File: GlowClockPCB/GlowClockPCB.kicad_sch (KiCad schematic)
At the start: 52 parts, among them J1 LED_OUT_1, J2 LED_OUT_2, J3 LED_OUT_3, J4 LED_OUT_4, J5 POWER_IN, J6 Motor_1_Out, J7 Motor_2_Out, J8 I2C_LCD, J9 ADC_OUT, SW1 BTN_UP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

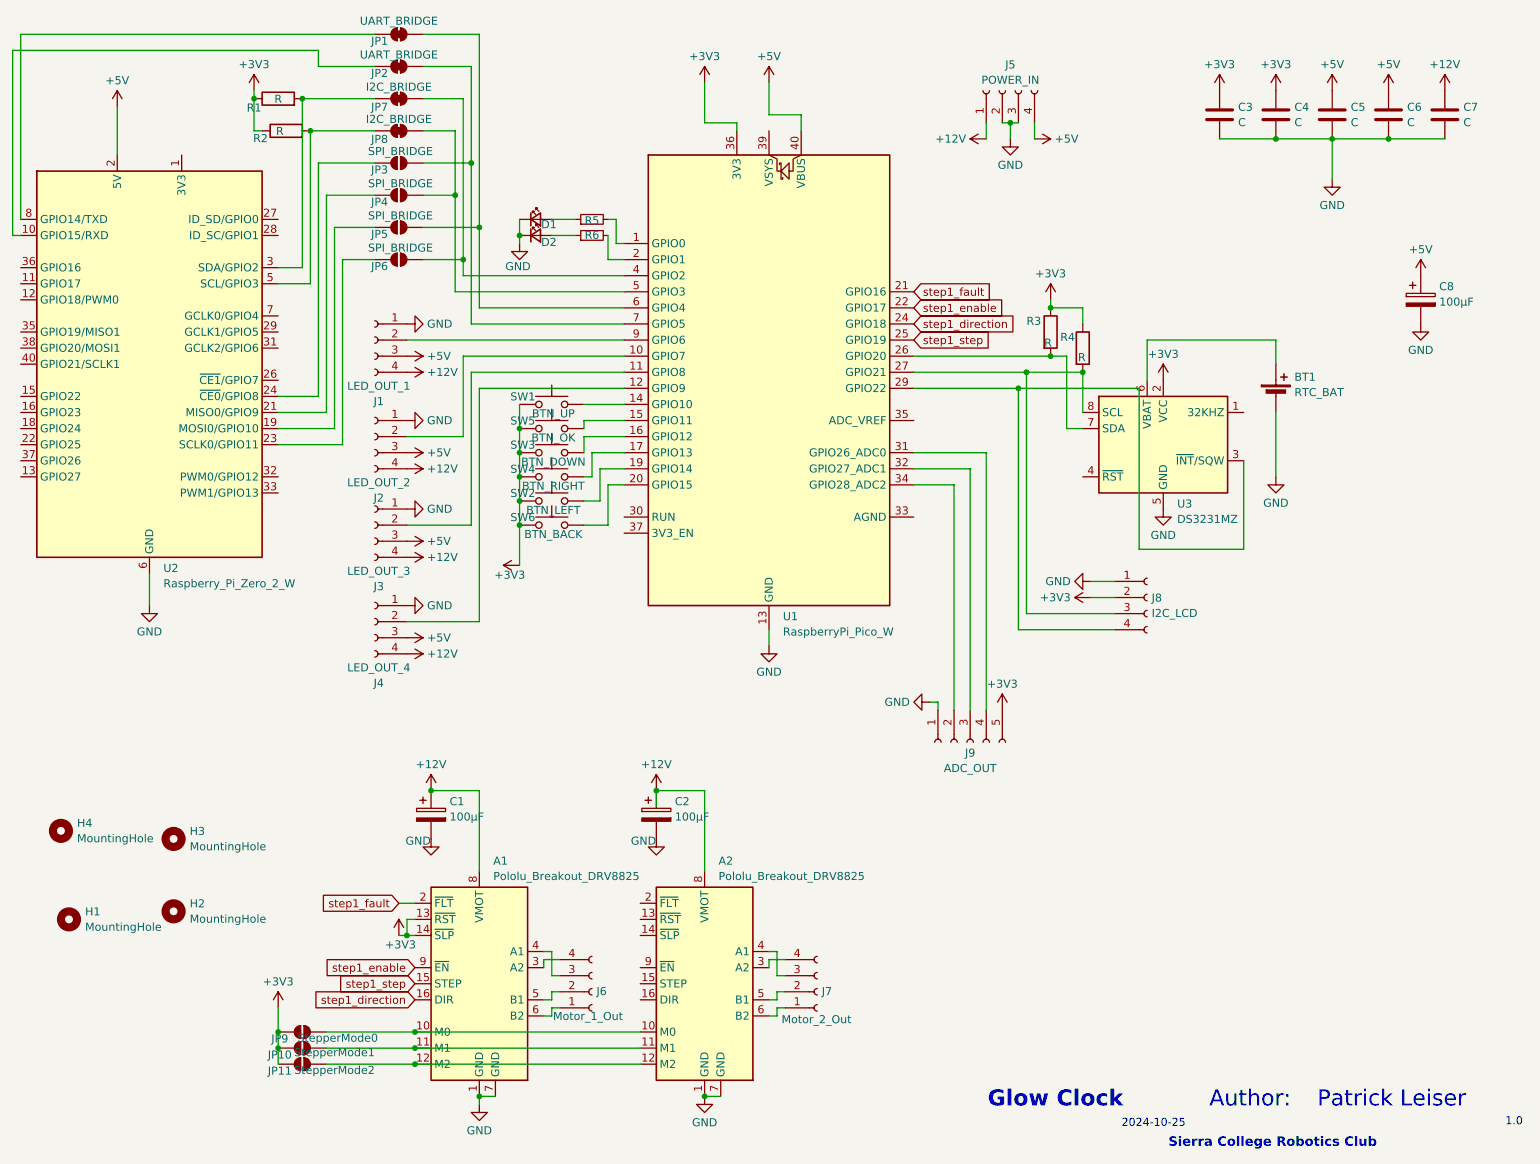
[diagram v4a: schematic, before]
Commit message: correct SDA connection for I2C_LCD port
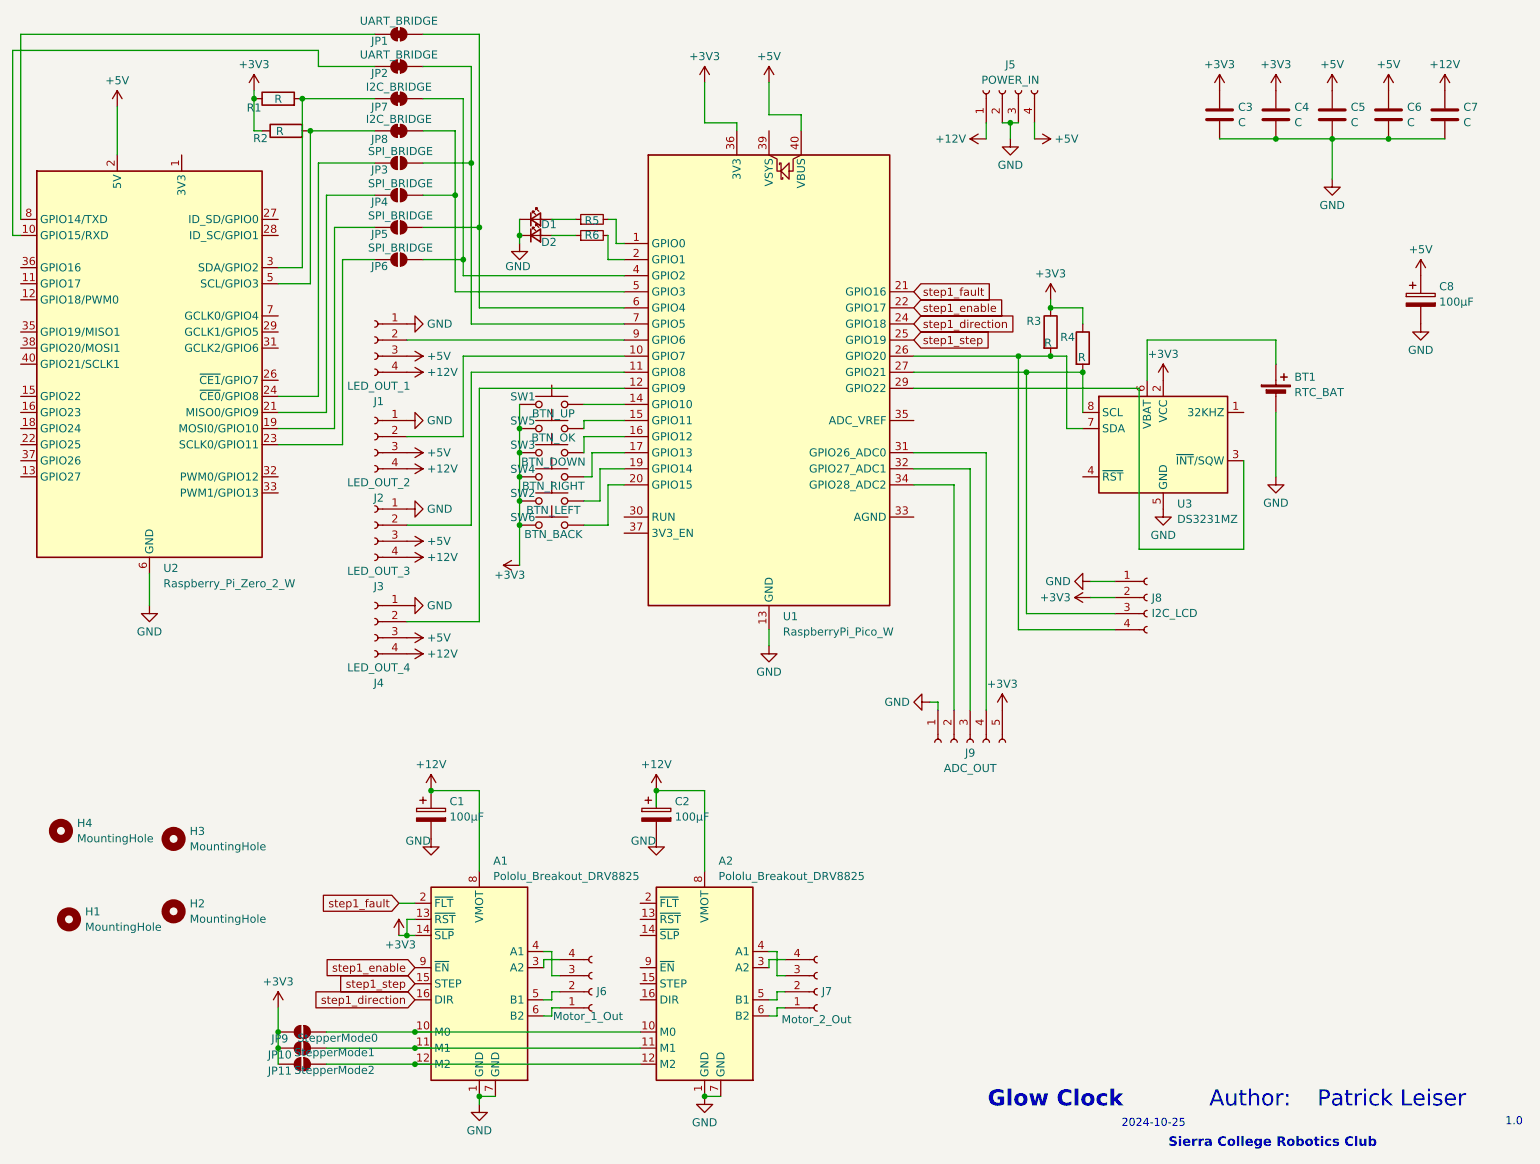
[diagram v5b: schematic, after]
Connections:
- net at R3.2, U1.26 (GPIO20), U3.7 (SDA): now also J8.4 (Pin_4)
- net at U1.29 (GPIO22), U3.3 (~{INT}/SQW): no longer J8.4 (Pin_4)
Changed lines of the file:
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@@
 (kicad_sch
-	(version 20231120)
+	(version 20250114)
 	(generator "eeschema")
-	(generator_version "8.0")
+	(generator_version "9.0")
 	(paper "A4")
+	(text "1.0"
+		(exclude_from_sim no)
+		(at 270.002 193.294 0)
+		(effects
+			(font
+				(size 1.27 1.27)
+			)
+		)
+	)
+	(text "Glow Clock"
+		(exclude_from_sim no)
+		(at 197.612 189.738 0)
+		(effects
+			(font
+				(size 2.54 2.54)
+				(thickness 0.508)
+				(bold yes)
+			)
+		)
+	)
+	(text "Author: "
+		(exclude_from_sim no)
+		(at 228.346 189.738 0)
+		(effects
+			(font
+				(size 2.54 2.54)
+				(color 132 0 0 1)
+			)
+		)
+	)
+	(text "Patrick Leiser"
+		(exclude_from_sim no)
+		(at 250.698 189.738 0)
+		(effects
+			(font
+				(size 2.54 2.54)
+			)
+		)
+	)
+	(text "Sierra College Robotics Club"
+		(exclude_from_sim no)
+		(at 231.902 196.596 0)
+		(effects
+			(font
+				(size 1.5 1.5)
+				(thickness 0.254)
+				(bold yes)
+			)
+		)
+	)
+	(text "2024-10-25"
+		(exclude_from_sim no)
+		(at 213.106 193.548 0)
+		(effects
+			(font
+				(size 1.27 1.27)
+			)
+		)
+	)
 	(junction
 		(at 113.03 87.63)
@@
 	)
 	(junction
+		(at 191.77 72.39)
+		(diameter 0)
+		(color 0 0 0 0)
+	)
+	(junction
 		(at 105.41 41.91)
 		(diameter 0)
@@
 	)
 	(junction
-		(at 191.77 77.47)
-		(diameter 0)
-		(color 0 0 0 0)
-	)
-	(junction
 		(at 232.41 38.1)
 		(diameter 0)
@@
 	(wire
 		(pts
-			(xy 191.77 77.47) (xy 210.82 77.47)
+			(xy 175.26 77.47) (xy 210.82 77.47)
 		)
 		(stroke
@@
 	(wire
 		(pts
-			(xy 175.26 77.47) (xy 191.77 77.47)
-		)
-		(stroke
-			(width 0)
-			(type default)
-		)
-	)
-	(wire
-		(pts
 			(xy 232.41 81.28) (xy 232.41 91.44)
 		)
@@
 	(wire
 		(pts
+			(xy 191.77 72.39) (xy 191.77 115.57)
+		)
+		(stroke
+			(width 0)
+			(type default)
+		)
+	)
+	(wire
+		(pts
 			(xy 189.23 35.56) (xy 190.5 35.56)
 		)
@@
 	(wire
 		(pts
-			(xy 175.26 72.39) (xy 196.85 72.39)
+			(xy 175.26 72.39) (xy 191.77 72.39)
 		)
 		(stroke
@@
 	(wire
 		(pts
-			(xy 191.77 77.47) (xy 191.77 115.57)
+			(xy 191.77 72.39) (xy 196.85 72.39)
 		)
 		(stroke
@@
 		)
 	)
-	(text "1.0"
-		(exclude_from_sim no)
-		(at 270.002 193.294 0)
-		(effects
-			(font
-				(size 1.27 1.27)
-			)
-		)
-	)
-	(text "Glow Clock"
-		(exclude_from_sim no)
-		(at 197.612 189.738 0)
-		(effects
-			(font
-				(size 2.54 2.54)
-				(thickness 0.508)
-				(bold yes)
-			)
-		)
-	)
-	(text "Author: "
-		(exclude_from_sim no)
-		(at 228.346 189.738 0)
-		(effects
-			(font
-				(size 2.54 2.54)
-				(color 132 0 0 1)
-			)
-		)
-	)
-	(text "Patrick Leiser"
-		(exclude_from_sim no)
-		(at 250.698 189.738 0)
-		(effects
-			(font
-				(size 2.54 2.54)
-			)
-		)
-	)
-	(text "Sierra College Robotics Club"
-		(exclude_from_sim no)
-		(at 231.902 196.596 0)
-		(effects
-			(font
-				(size 1.5 1.5)
-				(thickness 0.254)
-				(bold yes)
-			)
-		)
-	)
-	(text "2024-10-25"
-		(exclude_from_sim no)
-		(at 213.106 193.548 0)
-		(effects
-			(font
-				(size 1.27 1.27)
-			)
-		)
-	)
 	(global_label "step1_fault"
 		(shape input)
@@
 		)
 	)
+	(embedded_fonts no)
 )

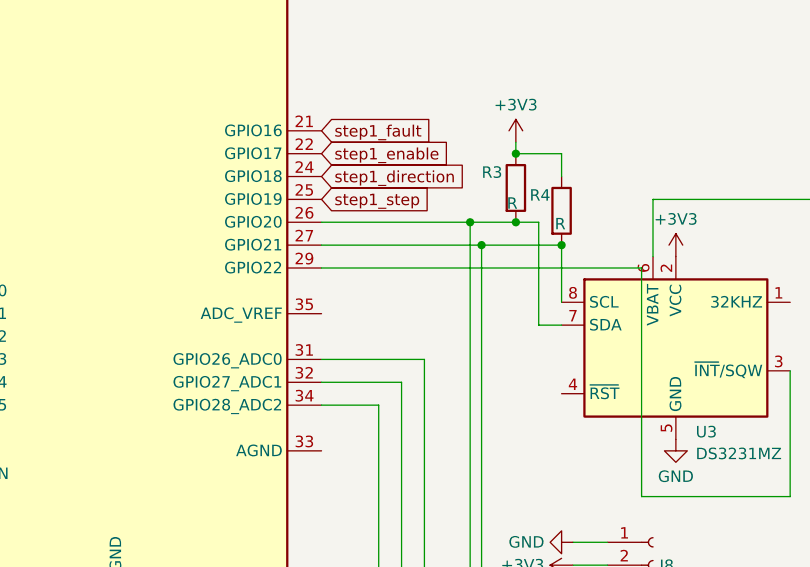
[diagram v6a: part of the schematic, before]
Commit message: update schematic to annotate v1 pcb errata, add ibom and svg schematic
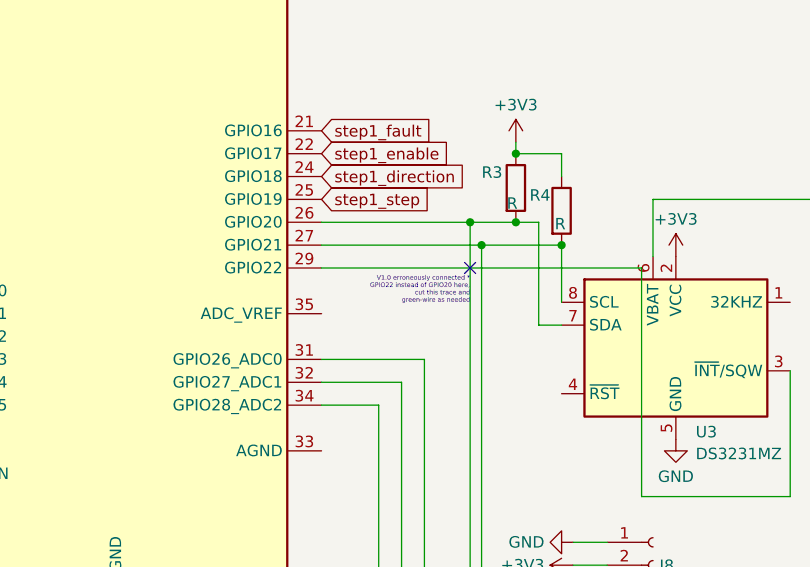
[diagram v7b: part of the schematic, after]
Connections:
- no-connect marks 0 -> 1
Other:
- note added: "V1.0 erroneously connected * GPIO22 instead of GPIO20 here, cut this trace and green-wire as needed"
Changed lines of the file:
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@@
+		)
+	)
+	(text "V1.0 erroneously connected *\nGPIO22 instead of GPIO20 here,  \ncut this trace and  \ngreen-wire as needed  "
+		(exclude_from_sim no)
+		(at 191.77 80.01 0)
+		(effects
+			(font
+				(size 0.508 0.508)
+			)
+			(justify right)
 		)
 	)
@@
 		(color 0 0 0 0)
 	)
+	(no_connect
+		(at 191.77 77.47)
+	)
 	(wire
